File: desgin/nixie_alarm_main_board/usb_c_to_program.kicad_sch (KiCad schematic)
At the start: 3 parts, among them J3 USB_C_Receptacle_USB2.0_16P

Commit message: filter caps
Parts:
- R3, R4: value 5.1k -> 5.1kΩ; footprint ERJUP6 -> RESC2012X60N
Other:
- moved on the sheet: R4
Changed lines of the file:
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@@
 	(wire
 		(pts
-			(xy 146.05 82.55) (xy 179.324 82.55)
+			(xy 146.05 82.55) (xy 180.848 82.55)
 		)
 		(stroke
@@
 	(wire
 		(pts
-			(xy 179.324 82.55) (xy 179.324 85.344)
+			(xy 180.848 82.55) (xy 180.848 85.344)
 		)
 		(stroke
@@
 	(symbol
 		(lib_id "power:GND")
-		(at 179.324 103.124 0)
+		(at 180.848 103.124 0)
 		(unit 1)
 		(exclude_from_sim no)
@@
 		(fields_autoplaced yes)
 		(property "Reference" "#PWR013"
-			(at 179.324 109.474 0)
+			(at 180.848 109.474 0)
 			(effects
 				(font
@@
 		)
 		(property "Value" "GND"
-			(at 179.324 108.204 0)
+			(at 180.848 108.204 0)
 			(effects
 				(font
@@
 		)
 		(property "Footprint" ""
-			(at 179.324 103.124 0)
+			(at 180.848 103.124 0)
 			(effects
 				(font
@@
 		)
 		(property "Datasheet" ""
-			(at 179.324 103.124 0)
+			(at 180.848 103.124 0)
 			(effects
 				(font
@@
 		)
 		(property "Description" "Power symbol creates a global label with name \"GND\" , ground"
-			(at 179.324 103.124 0)
+			(at 180.848 103.124 0)
 			(effects
 				(font
@@
 		(fields_autoplaced yes)
 		(property "Reference" "R3"
-			(at 172.974 92.7099 90)
+			(at 172.72 92.7099 90)
 			(effects
 				(font
@@
 			)
 		)
-		(property "Value" "5.1k"
-			(at 172.974 95.2499 90)
+		(property "Value" "5.1kΩ"
+			(at 172.72 95.2499 90)
 			(effects
 				(font
@@
 			)
 		)
-		(property "Footprint" "ERJUP6"
+		(property "Footprint" "RESC2012X60N"
 			(at 73.99 99.06 0)
 			(effects
@@
 	(symbol
 		(lib_id "SamacSys_Parts:ERJ-UP6D5101V")
-		(at 179.324 85.344 270)
+		(at 180.848 85.344 270)
 		(unit 1)
 		(exclude_from_sim no)
@@
 		(fields_autoplaced yes)
 		(property "Reference" "R4"
-			(at 181.61 92.9639 90)
+			(at 183.134 92.9639 90)
 			(effects
 				(font
@@
 			)
 		)
-		(property "Value" "5.1k"
-			(at 181.61 95.5039 90)
+		(property "Value" "5.1kΩ"
+			(at 183.134 95.5039 90)
 			(effects
 				(font
@@
 				)
 				(justify left)
-				(hide yes)
-			)
-		)
-		(property "Footprint" "ERJUP6"
-			(at 83.134 99.314 0)
+			)
+		)
+		(property "Footprint" "RESC2012X60N"
+			(at 84.658 99.314 0)
 			(effects
 				(font
@@
 		)
 		(property "Datasheet" "https://industrial.panasonic.com/cdbs/www-data/pdf/RDP0000/AOA0000C337.pdf"
-			(at -16.866 99.314 0)
+			(at -15.342 99.314 0)
 			(effects
 				(font
@@
 		)
 		(property "Description" "Anti-Sulfurated Thick Film Chip Resistors/ Anti-Surge Type, Power Rating (W): 0.5, Chip Size (LxW(EIA)) (mm): 2.0 x 1.25 (EIA:0805), Resistance Values (?): 5100, Resistance Tolerance (%): 0.5, T.C.R (?102/K): ?100"
-			(at 179.324 85.344 0)
+			(at 180.848 85.344 0)
 			(effects
 				(font
@@
 		)
 		(property "Height" "0.7"
-			(at -216.866 99.314 0)
+			(at -215.342 99.314 0)
 			(effects
 				(font
@@
 		)
 		(property "Mouser Part Number" "667-ERJ-UP6D5101V"
-			(at -316.866 99.314 0)
+			(at -315.342 99.314 0)
 			(effects
 				(font
@@
 		)
 		(property "Mouser Price/Stock" "https://www.mouser.co.uk/ProductDetail/Panasonic/ERJ-UP6D5101V?qs=ZcfC38r4Pouz7%2FLHthUDHQ%3D%3D"
-			(at -416.866 99.314 0)
+			(at -415.342 99.314 0)
 			(effects
 				(font
@@
 		)
 		(property "Manufacturer_Name" "Panasonic"
-			(at -516.866 99.314 0)
+			(at -515.342 99.314 0)
 			(effects
 				(font
@@
 		)
 		(property "Manufacturer_Part_Number" "ERJ-UP6D5101V"
-			(at -616.866 99.314 0)
-			(effects
-				(font
+			(at -615.342 99.314 0)
+			(effects
+				(font

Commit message: new rezistors
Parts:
- R3, R4: footprint RESC2012X60N -> Resistor_SMD:R_0805_2012Metric_Pad1.20x1.40mm_HandSolder
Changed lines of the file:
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@@
 			)
 		)
-		(property "Footprint" "RESC2012X60N"
+		(property "Footprint" "Resistor_SMD:R_0805_2012Metric_Pad1.20x1.40mm_HandSolder"
 			(at 73.99 99.06 0)
 			(effects
@@
 			)
 		)
-		(property "Footprint" "RESC2012X60N"
+		(property "Footprint" "Resistor_SMD:R_0805_2012Metric_Pad1.20x1.40mm_HandSolder"
 			(at 84.658 99.314 0)
 			(effects

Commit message: tvs protection try
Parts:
- added D1, D3: ESD7551N2T5G, ESD7551N2T5G, symbol Device:D_TVS
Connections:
- net GND: now also D1.1 (A1), D3.1 (A1)
- net USB_D+: now also D3.2 (A2)
- net USB_D-: now also D1.2 (A2)
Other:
- moved on the sheet: R3, R4

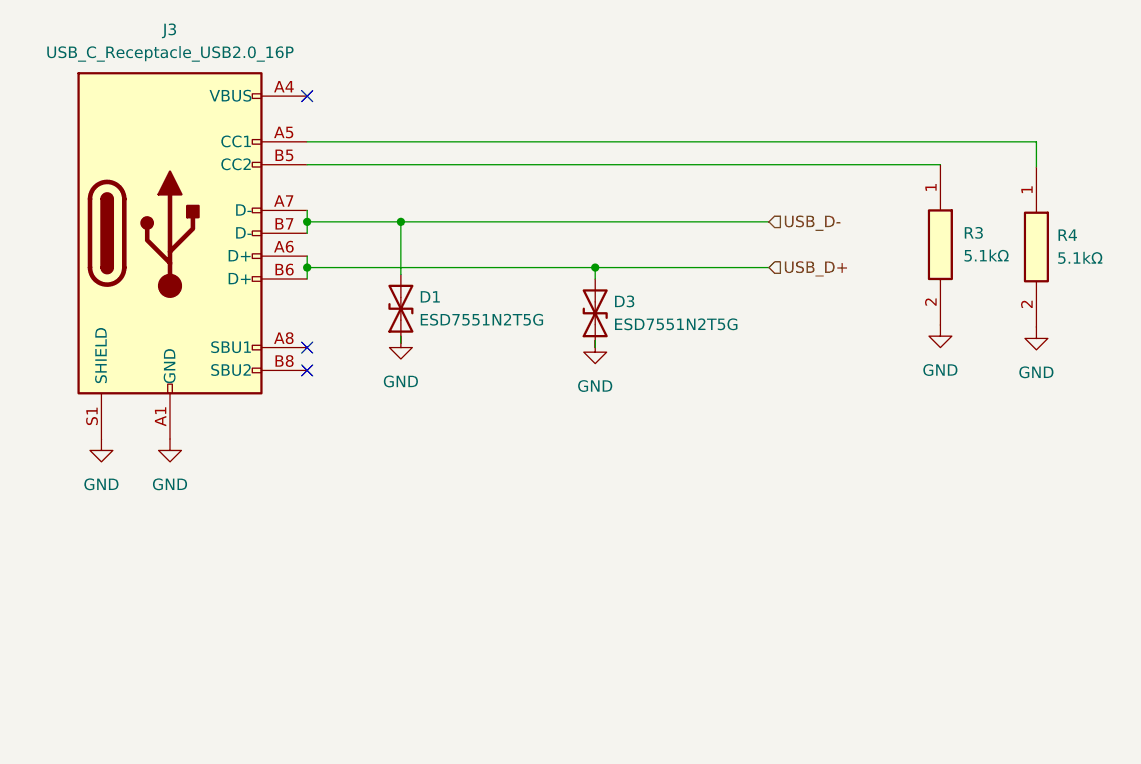
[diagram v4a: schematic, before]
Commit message: tvs added
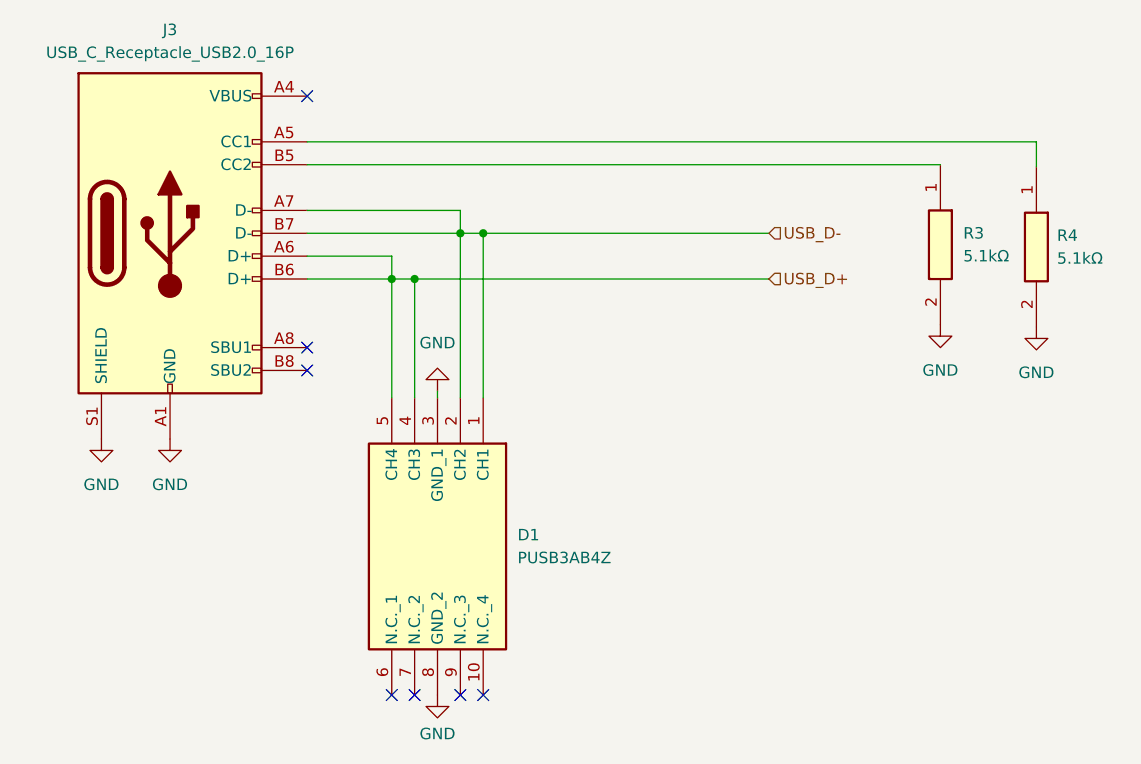
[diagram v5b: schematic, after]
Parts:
- removed D1, D3: ESD7551N2T5G, ESD7551N2T5G, symbol Device:D_TVS
- added D1: PUSB3AB4Z, SON50P100X250X50-10N, symbol SamacSys_Parts:PUSB3AB4Z
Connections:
- net GND: now also D1.3 (GND_1), D1.8 (GND_2)
- net USB_D+: now also D1.4 (CH3), D1.5 (CH4)
- net USB_D-: now also D1.1 (CH1), D1.2 (CH2)
- no-connect marks 3 -> 7
